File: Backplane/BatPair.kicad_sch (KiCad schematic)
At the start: 0 parts

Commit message: Done with two batteries
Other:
- added sheet BatMax - Female1 (BatMax - Female.kicad_sch)

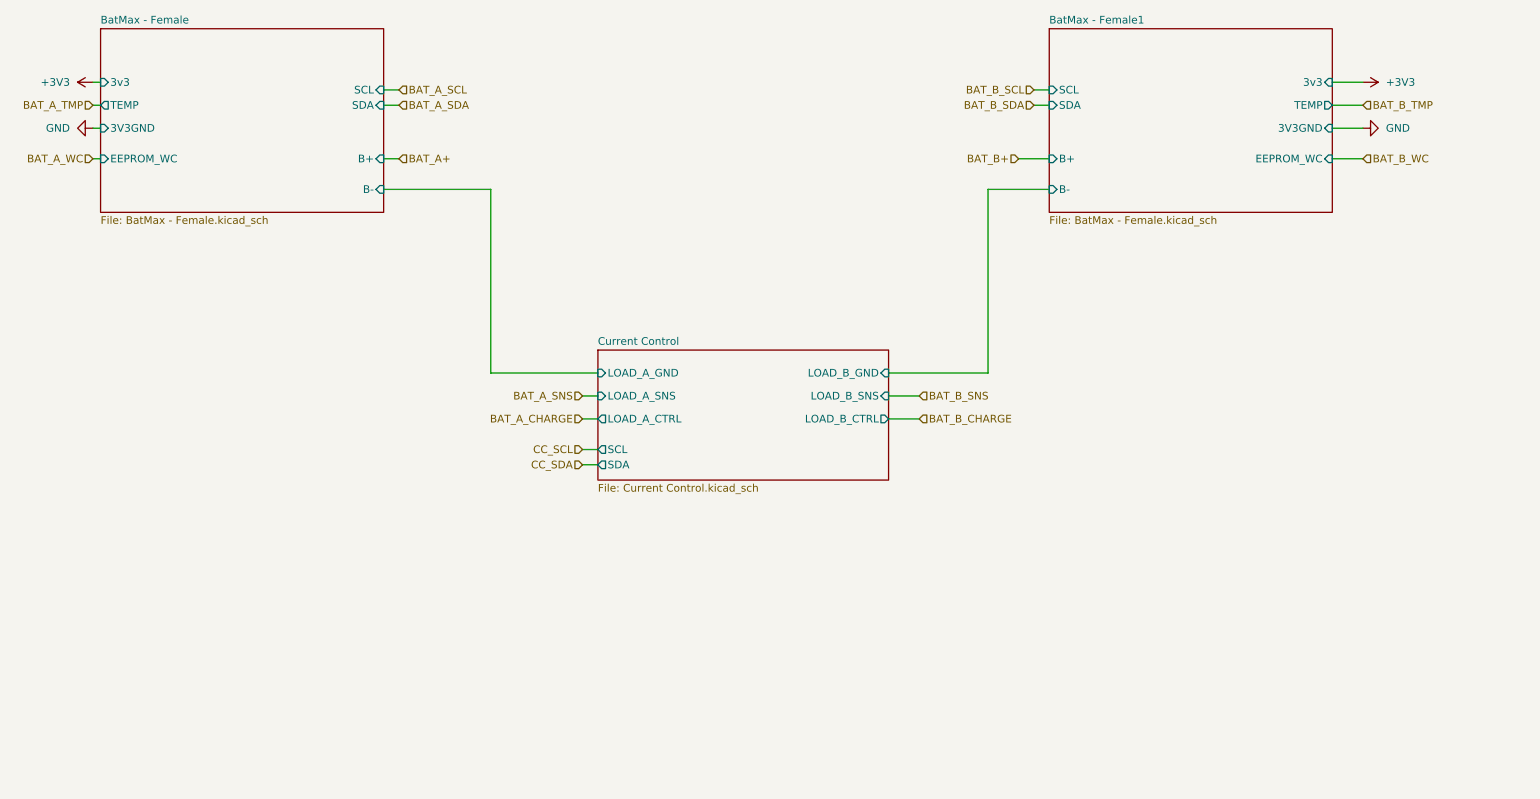
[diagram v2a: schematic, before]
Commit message: Working on splitting up I2C
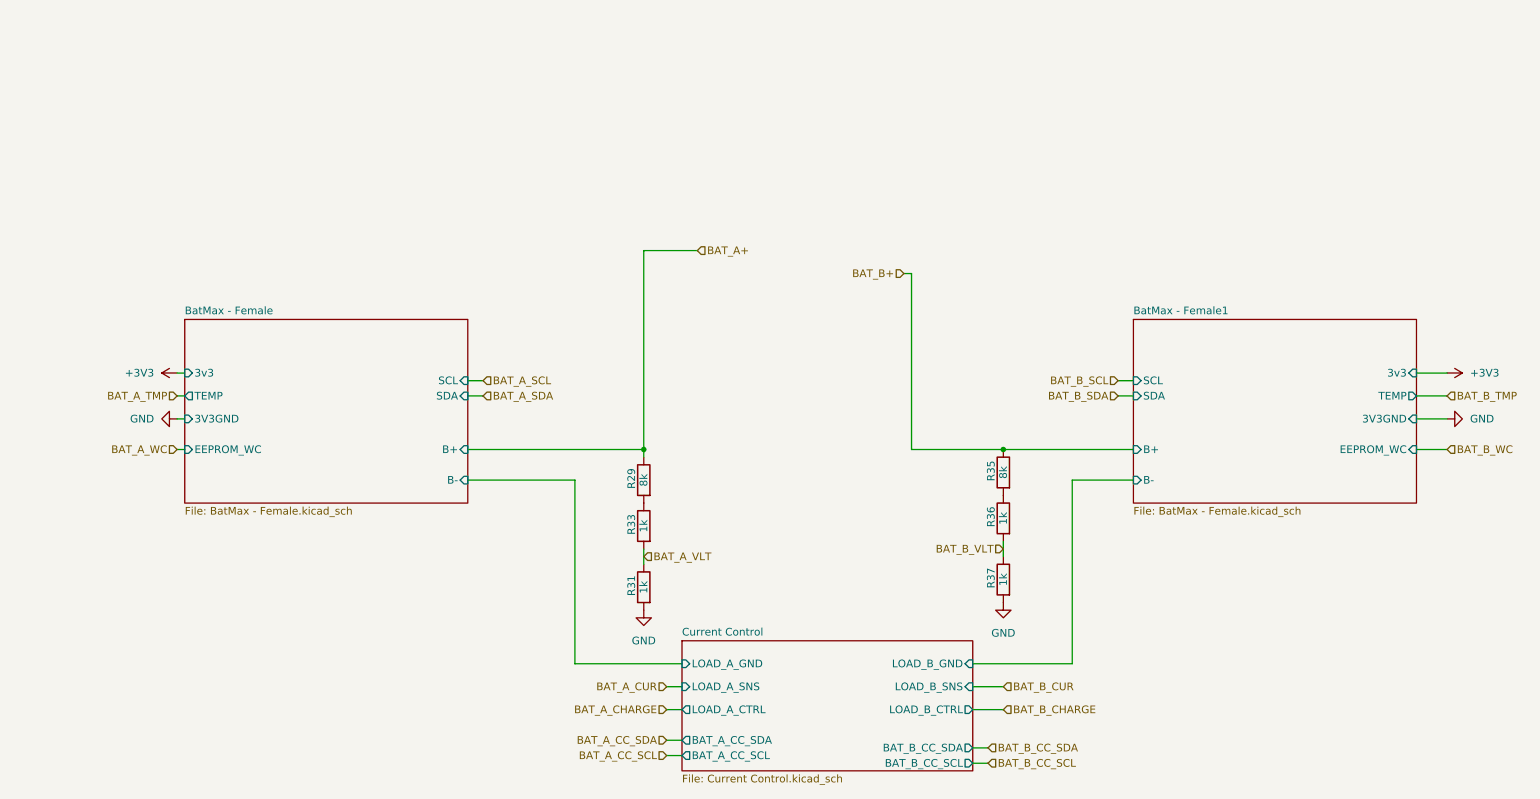
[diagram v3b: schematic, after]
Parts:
- added R29, R35: 8k, Resistor_SMD:R_1206_3216Metric_Pad1.30x1.75mm_HandSolder, symbol Device:R
- added R31, R33, R36, R37: 1k, Resistor_SMD:R_1206_3216Metric_Pad1.30x1.75mm_HandSolder, symbol Device:R
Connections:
- net BAT_A+: now also R29.1
- net BAT_B+: now also R35.1
- net GND: now also R31.2, R37.2
- new net: R35.2, R36.1
- new net: R29.2, R33.1
- new net BAT_A_VLT: R31.1, R33.2
- new net BAT_B_VLT: R36.2, R37.1
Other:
- sheet Current Control ports: added BAT_A_CC_SCL, BAT_A_CC_SDA, BAT_B_CC_SCL, BAT_B_CC_SDA; removed SCL, SDA
